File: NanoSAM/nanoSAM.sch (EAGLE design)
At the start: 90 parts, among them J1 POWER_JACK, U1 LTC3260EMSEPBF, U2 LMV324

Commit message: added some stuff, fixed some stuff
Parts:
- added C17, C18: 0.1uF, SparkFun-Capacitors:0.1UF-0603-25V-5%
- added C19, C20: .1uF, SparkFun-Capacitors:0.1UF-0603-25V-5%
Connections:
- net +3V3: now also C19.1, C20.2
- net -5V: now also C18.1
- net 5V: now also C17.1
- net AGND: now also C17.2, C18.2
- net DGND: now also C19.2, C20.1
- net SPI_MISO: now also U$16.SO, U$17.SO; no longer U$16.SI, U$17.SI
- net SPI_MOSI: now also U$16.SI, U$17.SI; no longer U$16.SCK, U$17.SCK
- net SPI_SCK: now also U$16.SCK, U$17.SCK; no longer U$16.SO, U$17.SO
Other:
- moved on the sheet: C1, R25

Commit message: updated some stuff
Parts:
- C1: value 0.1uF -> 100pF
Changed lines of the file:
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@@
 <part name="U$1" library="photodiodesymbol" deviceset="PHOTODIODESYMBOL" device="PD_CONN" value="PHOTODIODESYMBOLPD_CONN"/>
 <part name="R2" library="SparkFun-Resistors" library_urn="urn:adsk.eagle:library:532" deviceset="RESISTOR" device="0805" package3d_urn="urn:adsk.eagle:package:39651/1" value=" "/>
-<part name="C1" library="SparkFun-Capacitors" library_urn="urn:adsk.eagle:library:510" deviceset="0.1UF" device="-0603-25V-5%" package3d_urn="urn:adsk.eagle:package:37414/1" value="0.1uF"/>
+<part name="C1" library="SparkFun-Capacitors" library_urn="urn:adsk.eagle:library:510" deviceset="0.1UF" device="-0603-25V-5%" package3d_urn="urn:adsk.eagle:package:37414/1" value="100pF"/>
 <part name="C3" library="SparkFun-Capacitors" library_urn="urn:adsk.eagle:library:510" deviceset="0.1UF" device="-0603-25V-5%" package3d_urn="urn:adsk.eagle:package:37414/1" value="0.1uF"/>
 <part name="R4" library="SparkFun-Resistors" library_urn="urn:adsk.eagle:library:532" deviceset="RESISTOR" device="0805" package3d_urn="urn:adsk.eagle:package:39651/1" value=" "/>

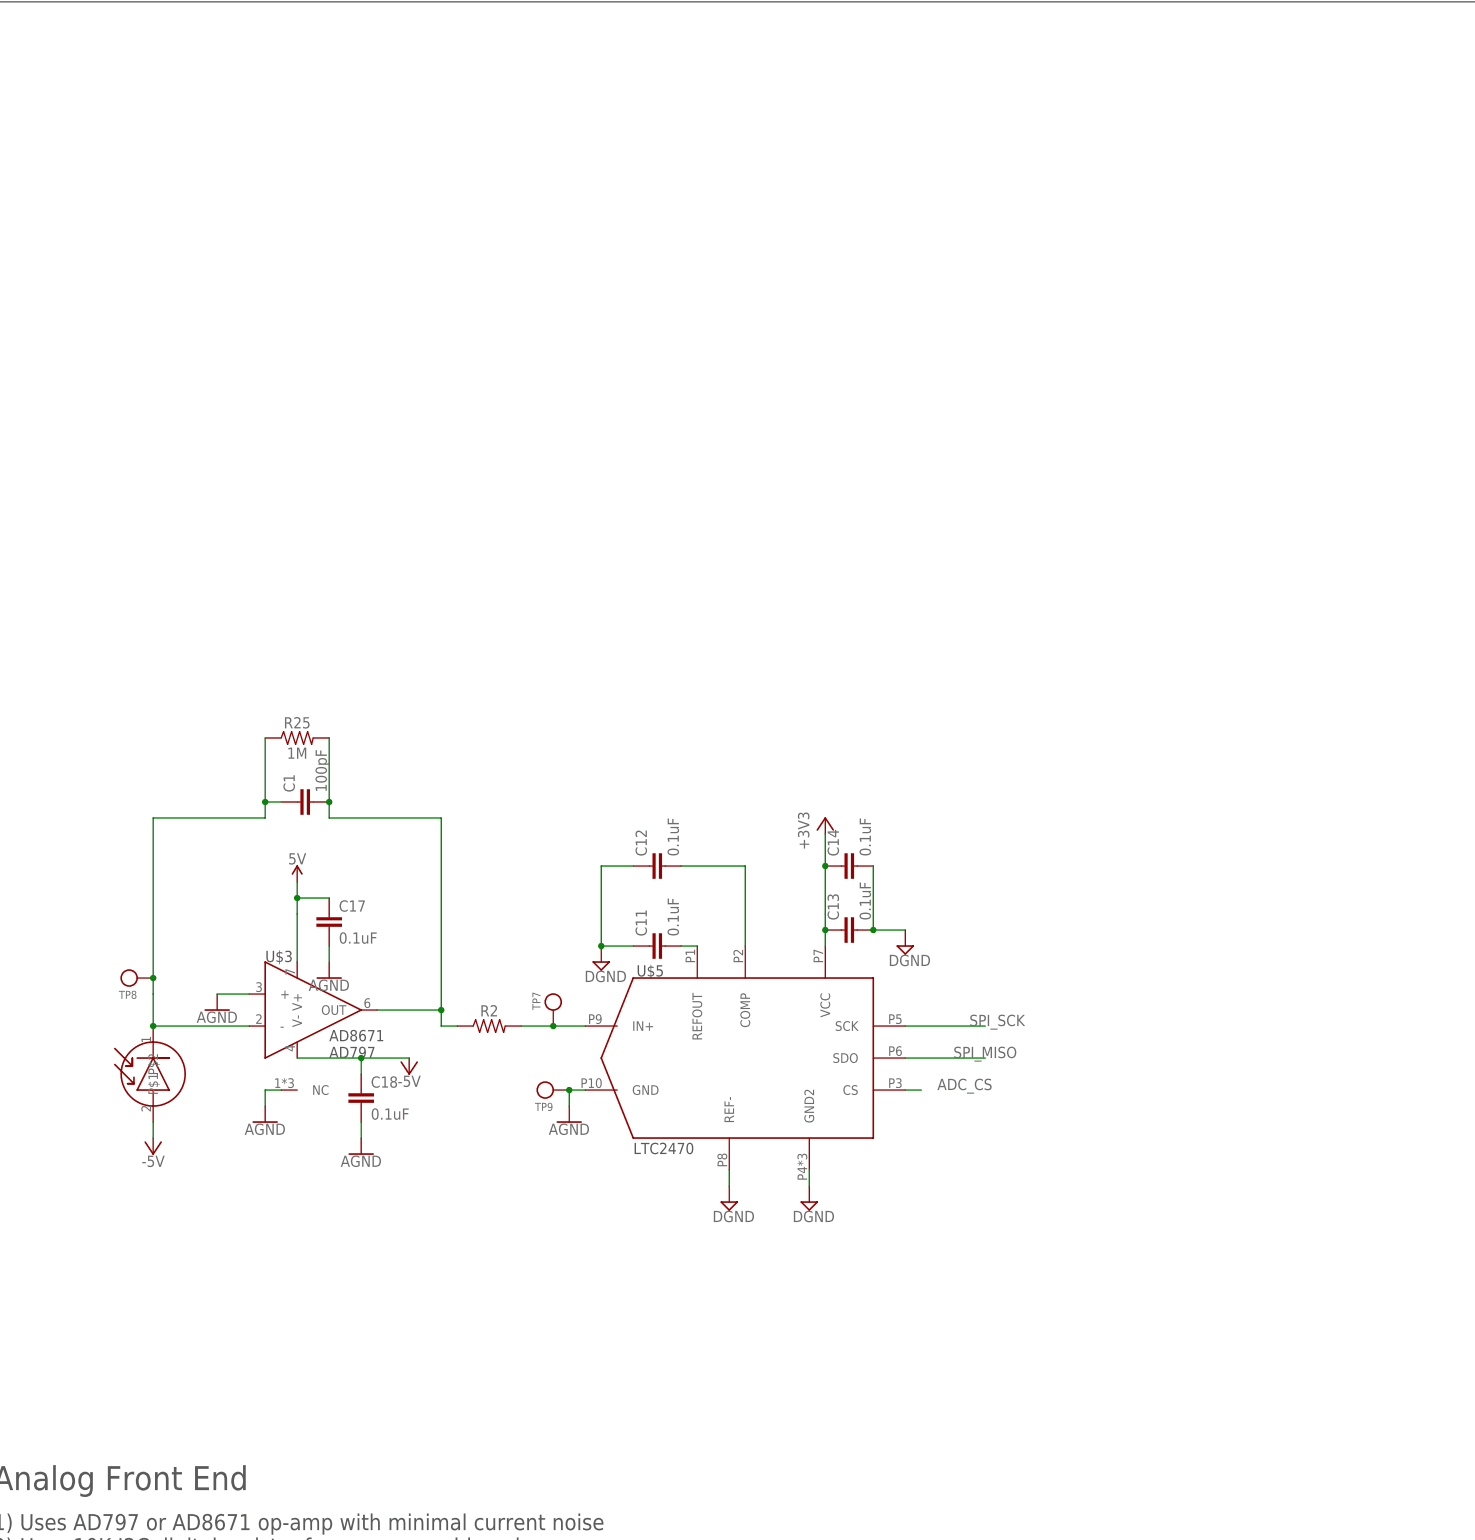
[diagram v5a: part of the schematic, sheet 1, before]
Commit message: added options for grounding ADCs
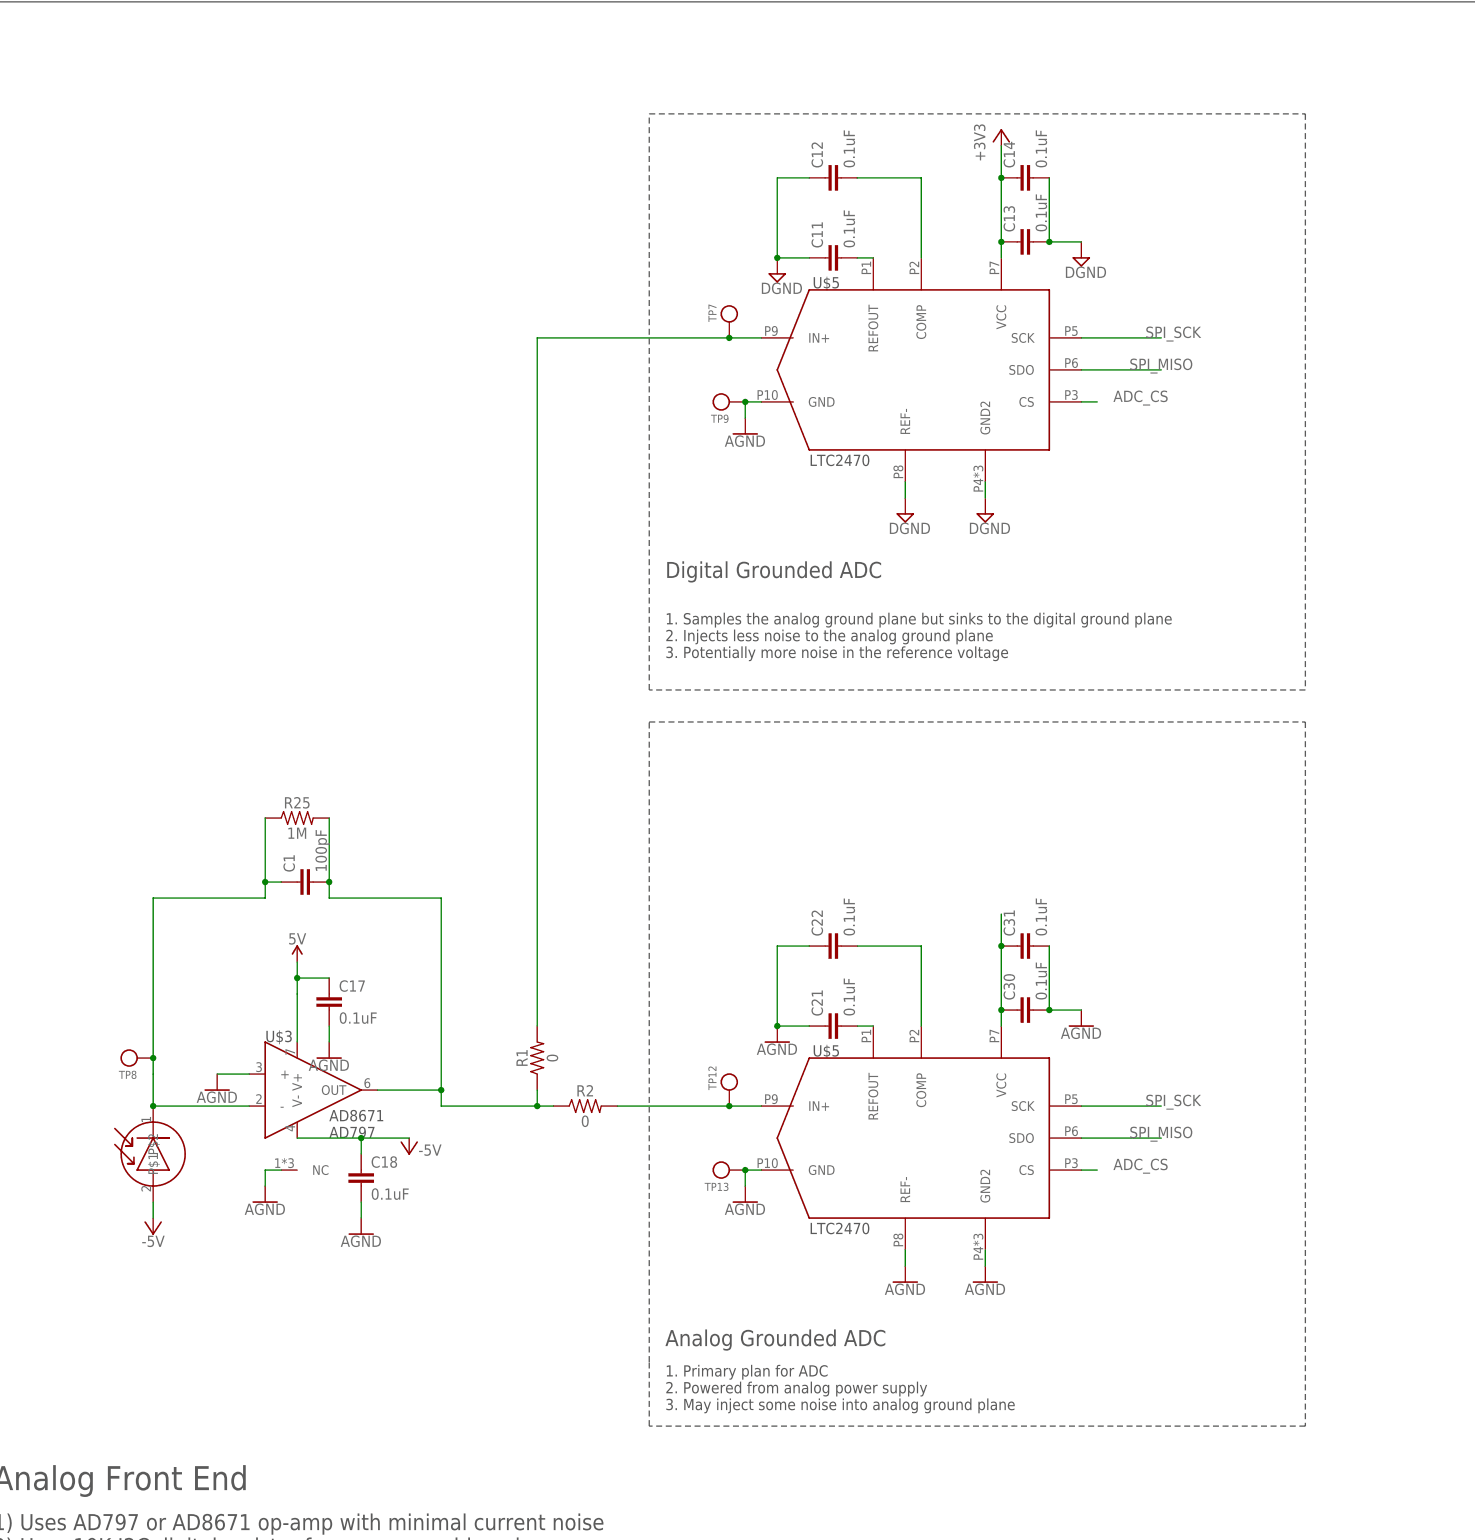
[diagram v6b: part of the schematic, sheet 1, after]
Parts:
- added C21, C22, C30, C31: 0.1uF, SparkFun-Capacitors:0.1UF-0603-25V-5%
- added R1: 0, SparkFun-Resistors:RESISTOR0805
- added TP12, TP13: (no value), testpoint:TESTPOINT
- added U$26: LTC2470, LTC2470:LTC2470
- R2: value (none) -> 0
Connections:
- new net N$25: C21.2, U$26.REFOUT
- new net N$26: C30.1, C31.1, U$26.VCC
- new net N$5: R2.2, TP12.P$1, U$26.IN+
- new net N$9: C22.2, U$26.COMP
- net ADC_CS: now also U$26.CS
- net AGND: now also C21.1, C22.1, C30.2, C31.2, TP13.P$1, U$26.GND, U$26.GND2, U$26.REF-
- net N$2: now also R1.1
- net N$3: now also R1.2; no longer R2.2
- net SPI_MISO: now also U$26.SDO
- net SPI_SCK: now also U$26.SCK
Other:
- note added: "1. Primary plan for ADC 2. Powered from analog power supply 3. May inject some noise into analog ground plane"
- note added: "1. Samples the analog ground plane but sinks to the digital ground plane 2. Injects less noise to the analog ground plane 3. Potentially more noise in the reference voltage"
- note added: "Analog Grounded ADC"
- note added: "Digital Grounded ADC"
- moved on the sheet: C1, C11, C12, C13, C14, C17, C18, R2, R25, TP7, TP8, TP9
